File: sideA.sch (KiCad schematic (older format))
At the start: 16 parts

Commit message: Annotations and ERC error pending
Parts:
- gave numbers to parts that had none: 16
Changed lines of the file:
@@
-EESchema Schematic File Version 2  date Sun 16 Sep 2012 06:59:06 AM PDT
+EESchema Schematic File Version 2  date Tue 18 Sep 2012 12:09:37 PM PDT
 LIBS:power
 LIBS:device
@@
 Sheet 1 1
 Title "SMT4dummies - sideA"
-Date "16 sep 2012"
+Date "18 sep 2012"
 Rev ""
 Comp "d-Squared Robotics"
@@
 Comment4 ""
 $EndDescr
+Wire Wire Line
+	3550 2100 3650 2100
+Wire Bus Line
+	800  3300 800  800
+Wire Bus Line
+	800  3300 3000 3300
+Wire Bus Line
+	800  800  3000 800
+Wire Wire Line
+	1150 1050 2650 1050
+Wire Wire Line
+	5650 1150 5650 1050
+Connection ~ 4150 3650
+Wire Wire Line
+	4150 3650 4150 3000
+Connection ~ 5250 3650
+Wire Wire Line
+	5250 3550 5250 3650
+Wire Wire Line
+	3650 3650 5650 3650
+Connection ~ 4500 2300
+Wire Wire Line
+	4500 2950 4500 2300
+Wire Wire Line
+	3850 2800 3750 2800
+Wire Wire Line
+	3750 2800 3750 2300
+Wire Wire Line
+	3750 2300 4600 2300
+Wire Wire Line
+	5650 1550 5650 1650
+Wire Wire Line
+	5100 2500 5250 2500
+Wire Wire Line
+	5350 2800 5250 2800
+Connection ~ 4150 2500
+Connection ~ 1650 3050
+Wire Wire Line
+	1650 2950 1650 3050
+Wire Wire Line
+	2650 1650 2650 1550
+Wire Wire Line
+	2250 2450 2350 2450
+Wire Wire Line
+	1650 2150 1650 2550
+Wire Wire Line
+	1050 1850 1150 1850
+Wire Wire Line
+	1150 1850 1150 1050
+Wire Wire Line
+	2650 1050 2650 1150
+Wire Wire Line
+	1650 1550 1650 1050
+Connection ~ 1650 1050
+Wire Wire Line
+	1750 2450 1650 2450
+Connection ~ 1650 2450
+Wire Wire Line
+	2650 2250 2650 2150
+Wire Wire Line
+	2650 2650 2650 3050
+Wire Wire Line
+	1150 2050 1150 3050
+Wire Wire Line
+	1150 2050 1000 2050
+Wire Wire Line
+	4150 2150 4150 2600
+Wire Wire Line
+	4150 1550 4150 1650
+Wire Wire Line
+	5100 2300 5650 2300
+Wire Wire Line
+	5650 2150 5650 2600
+Connection ~ 5650 2300
+Wire Wire Line
+	5250 2500 5250 2950
+Connection ~ 5250 2800
+Wire Wire Line
+	3650 3650 3650 2300
+Wire Wire Line
+	5650 3650 5650 3000
+Wire Wire Line
+	4500 3550 4500 3650
+Connection ~ 4500 3650
+Wire Wire Line
+	4150 1050 4150 1150
+Wire Wire Line
+	1150 3050 2650 3050
+Wire Wire Line
+	4600 2500 4150 2500
+Wire Wire Line
+	3650 2100 3650 1050
+Wire Wire Line
+	3650 1050 5650 1050
+Connection ~ 4150 1050
+Wire Bus Line
+	3000 800  3000 3300
+Wire Bus Line
+	3300 3900 6050 3900
+Wire Bus Line
+	3300 3900 3300 800
+Wire Bus Line
+	6050 3900 6050 800
 Wire Bus Line
 	6050 800  3300 800
-Wire Bus Line
-	6050 800  6050 3900
-Wire Bus Line
-	3300 800  3300 3900
-Wire Bus Line
-	3300 3900 6050 3900
-Wire Bus Line
-	3000 800  3000 3300
-Connection ~ 4150 1050
-Wire Wire Line
-	3650 1050 5650 1050
-Wire Wire Line
-	3500 2300 3650 2300
-Wire Wire Line
-	3650 1050 3650 2100
-Wire Wire Line
-	4600 2500 4150 2500
-Wire Wire Line
-	1150 3050 2650 3050
-Wire Wire Line
-	4150 1050 4150 1150
-Connection ~ 4500 3650
-Wire Wire Line
-	4500 3550 4500 3650
-Wire Wire Line
-	5650 3000 5650 3650
-Wire Wire Line
-	3650 2300 3650 3650
-Connection ~ 5250 2800
-Wire Wire Line
-	5250 2950 5250 2500
-Connection ~ 5650 2300
-Wire Wire Line
-	5650 2150 5650 2600
-Wire Wire Line
-	5100 2300 5650 2300
-Wire Wire Line
-	4150 1550 4150 1650
-Wire Wire Line
-	4150 2150 4150 2600
-Wire Wire Line
-	1000 2050 1150 2050
-Wire Wire Line
-	1150 2050 1150 3050
-Wire Wire Line
-	2650 3050 2650 2650
-Wire Wire Line
-	2650 2250 2650 2150
-Connection ~ 1650 2450
-Wire Wire Line
-	1750 2450 1650 2450
-Connection ~ 1650 1050
-Wire Wire Line
-	1650 1550 1650 1050
-Wire Wire Line
-	2650 1150 2650 1050
-Wire Wire Line
-	1150 1850 1150 1050
-Wire Wire Line
-	1150 1850 1050 1850
-Wire Wire Line
-	1650 2150 1650 2550
-Wire Wire Line
-	2250 2450 2350 2450
-Wire Wire Line
-	2650 1650 2650 1550
-Wire Wire Line
-	1650 2950 1650 3050
-Connection ~ 1650 3050
-Connection ~ 4150 2500
-Wire Wire Line
-	5350 2800 5250 2800
-Wire Wire Line
-	5250 2500 5100 2500
-Wire Wire Line
-	5650 1550 5650 1650
-Wire Wire Line
-	4600 2300 3750 2300
-Wire Wire Line
-	3750 2300 3750 2800
-Wire Wire Line
-	3750 2800 3850 2800
-Wire Wire Line
-	4500 2950 4500 2300
-Connection ~ 4500 2300
-Wire Wire Line
-	3650 3650 5650 3650
-Wire Wire Line
-	5250 3550 5250 3650
-Connection ~ 5250 3650
-Wire Wire Line
-	4150 3650 4150 3000
-Connection ~ 4150 3650
-Wire Wire Line
-	5650 1050 5650 1150
-Wire Wire Line
-	1150 1050 2650 1050
-Wire Wire Line
-	3650 2100 3550 2100
-Wire Bus Line
-	3000 800  800  800
-Wire Bus Line
-	3000 3300 800  3300
-Wire Bus Line
-	800  3300 800  800
+Wire Wire Line
+	3650 2300 3500 2300
 Text Notes 5600 3850 0    60   ~ 0
 Memory\n
 $Comp
-L SW_PUSH SW?
+L SW_PUSH SW2
 U 1 1 5055BB35
 P 4500 3250
-F 0 "SW?" H 4650 3360 50  0000 C CNN
+F 0 "SW2" H 4650 3360 50  0000 C CNN
 F 1 "SW_PUSH" H 4500 3170 50  0000 C CNN
 	1    4500 3250
@@
 $EndComp
 $Comp
-L SW_PUSH SW?
+L SW_PUSH SW3
 U 1 1 5055BB28
 P 5250 3250
-F 0 "SW?" H 5400 3360 50  0000 C CNN
+F 0 "SW3" H 5400 3360 50  0000 C CNN
 F 1 "SW_PUSH" H 5250 3170 50  0000 C CNN
 	1    5250 3250
@@
 $EndComp
 $Comp
-L R R?
+L R R4
 U 1 1 5055B3BC
 P 4850 2300
-F 0 "R?" V 4930 2300 50  0000 C CNN
+F 0 "R4" V 4930 2300 50  0000 C CNN
 F 1 "R" V 4850 2300 50  0000 C CNN
 	1    4850 2300
@@
 $EndComp
 $Comp
-L R R?
+L R R5
 U 1 1 5055B3AE
 P 4850 2500
-F 0 "R?" V 4930 2500 50  0000 C CNN
+F 0 "R5" V 4930 2500 50  0000 C CNN
 F 1 "R" V 4850 2500 50  0000 C CNN
 	1    4850 2500
@@
 $EndComp
 $Comp
-L BC237 Q?
+L BC237 Q3
 U 1 1 5055B0D0
 P 5550 2800
-F 0 "Q?" H 5750 2700 50  0000 C CNN
+F 0 "Q3" H 5750 2700 50  0000 C CNN
 F 1 "BC237" H 5800 2950 50  0000 C CNN
 F 2 "TO92-EBC" H 5740 2800 30  0001 C CNN
@@
 $EndComp
 $Comp
-L BC237 Q?
+L BC237 Q2
 U 1 1 5055B0B6
 P 4050 2800
-F 0 "Q?" H 4250 2700 50  0000 C CNN
+F 0 "Q2" H 4250 2700 50  0000 C CNN
 F 1 "BC237" H 4300 2950 50  0000 C CNN
 F 2 "TO92-EBC" H 4240 2800 30  0001 C CNN
@@
 $EndComp
 $Comp
-L R R?
+L R R6
 U 1 1 5055AFCE
 P 5650 1900
-F 0 "R?" V 5730 1900 50  0000 C CNN
+F 0 "R6" V 5730 1900 50  0000 C CNN
 F 1 "R" V 5650 1900 50  0000 C CNN
 	1    5650 1900
@@
 $EndComp
 $Comp
-L R R?
+L R R3
 U 1 1 5055AFCA
 P 4150 1900
-F 0 "R?" V 4230 1900 50  0000 C CNN
+F 0 "R3" V 4230 1900 50  0000 C CNN
 F 1 "R" V 4150 1900 50  0000 C CNN
 	1    4150 1900
@@
 $EndComp
 $Comp
-L LED D?
+L LED D3
 U 1 1 5055AFBC
 P 5650 1350
-F 0 "D?" H 5650 1450 50  0000 C CNN
+F 0 "D3" H 5650 1450 50  0000 C CNN
 F 1 "LED" H 5650 1250 50  0000 C CNN
 	1    5650 1350
@@
 $EndComp
 $Comp
-L LED D?
+L LED D2
 U 1 1 5051E656
 P 4150 1350
-F 0 "D?" H 4150 1450 50  0000 C CNN
+F 0 "D2" H 4150 1450 50  0000 C CNN
 F 1 "LED" H 4150 1250 50  0000 C CNN
 	1    4150 1350
@@
 $EndComp
 $Comp
-L R R?
+L R R1
 U 1 1 5051AD8C
 P 2000 2450
-F 0 "R?" V 2080 2450 50  0000 C CNN
+F 0 "R1" V 2080 2450 50  0000 C CNN
 F 1 "R" V 2000 2450 50  0000 C CNN
 	1    2000 2450
@@
 $EndComp
 $Comp
-L BC237 Q?
+L BC237 Q1
 U 1 1 5051AD26
 P 2550 2450
-F 0 "Q?" H 2750 2350 50  0000 C CNN
+F 0 "Q1" H 2750 2350 50  0000 C CNN
 F 1 "BC237" H 2800 2600 50  0000 C CNN
 F 2 "TO92-EBC" H 2740 2450 30  0001 C CNN
@@
 $EndComp
 $Comp
-L SW_PUSH SW?
+L SW_PUSH SW1
 U 1 1 5051AC01
 P 1650 1850
-F 0 "SW?" H 1800 1960 50  0000 C CNN
+F 0 "SW1" H 1800 1960 50  0000 C CNN
 F 1 "SW_PUSH" H 1650 1770 50  0000 C CNN
 	1    1650 1850
@@
 $EndComp
 $Comp
-L LED D?
+L LED D1
 U 1 1 5051A946
 P 2650 1350
-F 0 "D?" H 2650 1450 50  0000 C CNN
+F 0 "D1" H 2650 1450 50  0000 C CNN
 F 1 "LED" H 2650 1250 50  0000 C CNN
 	1    2650 1350
@@
 $EndComp
 $Comp
-L CP1 C?
+L CP1 C1
 U 1 1 5051A92A
 P 1650 2750
-F 0 "C?" H 1700 2850 50  0000 L CNN
+F 0 "C1" H 1700 2850 50  0000 L CNN
 F 1 "CP1" H 1700 2650 50  0000 L CNN
 	1    1650 2750
@@
 $EndComp
 $Comp
-L R R?
+L R R2
 U 1 1 5051A90B
 P 2650 1900
-F 0 "R?" V 2730 1900 50  0000 C CNN
+F 0 "R2" V 2730 1900 50  0000 C CNN
 F 1 "R" V 2650 1900 50  0000 C CNN
 	1    2650 1900

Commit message: Annotated and ERC checked
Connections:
- wire segments 40 -> 42
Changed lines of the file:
@@
-EESchema Schematic File Version 2  date Tue 18 Sep 2012 12:09:37 PM PDT
+EESchema Schematic File Version 2  date Tue 18 Sep 2012 12:41:14 PM PDT
 LIBS:power
 LIBS:device
@@
 Comment4 ""
 $EndDescr
-Wire Wire Line
-	3550 2100 3650 2100
+Wire Bus Line
+	6300 1450 6300 800
+Wire Bus Line
+	6300 1450 6850 1450
+Wire Bus Line
+	6850 1450 6850 800
+Wire Bus Line
+	6850 800  6300 800
+Wire Wire Line
+	6450 1100 6450 1200
+Wire Wire Line
+	3500 2300 3650 2300
+Wire Bus Line
+	6050 800  3300 800
+Wire Bus Line
+	6050 800  6050 3900
+Wire Bus Line
+	3300 800  3300 3900
+Wire Bus Line
+	3300 3900 6050 3900
+Wire Bus Line
+	3000 800  3000 3300
+Connection ~ 4150 1050
+Wire Wire Line
+	3650 1050 5650 1050
+Wire Wire Line
+	3650 1050 3650 2100
+Wire Wire Line
+	4600 2500 4150 2500
+Wire Wire Line
+	1150 3050 2650 3050
+Wire Wire Line
+	4150 1050 4150 1150
+Connection ~ 4500 3650
+Wire Wire Line
+	4500 3550 4500 3650
+Wire Wire Line
+	5650 3000 5650 3650
+Wire Wire Line
+	3650 2300 3650 3650
+Connection ~ 5250 2800
+Wire Wire Line
+	5250 2950 5250 2500
+Connection ~ 5650 2300
+Wire Wire Line
+	5650 2150 5650 2600
+Wire Wire Line
+	5100 2300 5650 2300
+Wire Wire Line
+	4150 1550 4150 1650
+Wire Wire Line
+	4150 2150 4150 2600
+Wire Wire Line
+	1000 2050 1150 2050
+Wire Wire Line
+	1150 2050 1150 3050
+Wire Wire Line
+	2650 3050 2650 2650
+Wire Wire Line
+	2650 2250 2650 2150
+Connection ~ 1650 2450
+Wire Wire Line
+	1750 2450 1650 2450
+Connection ~ 1650 1050
+Wire Wire Line
+	1650 1550 1650 1050
+Wire Wire Line
+	2650 1150 2650 1050
+Wire Wire Line
+	1150 1850 1150 1050
+Wire Wire Line
+	1150 1850 1050 1850
+Wire Wire Line
+	1650 2150 1650 2550
+Wire Wire Line
+	2250 2450 2350 2450
+Wire Wire Line
+	2650 1650 2650 1550
+Wire Wire Line
+	1650 2950 1650 3050
+Connection ~ 1650 3050
+Connection ~ 4150 2500
+Wire Wire Line
+	5350 2800 5250 2800
+Wire Wire Line
+	5250 2500 5100 2500
+Wire Wire Line
+	5650 1550 5650 1650
+Wire Wire Line
+	4600 2300 3750 2300
+Wire Wire Line
+	3750 2300 3750 2800
+Wire Wire Line
+	3750 2800 3850 2800
+Wire Wire Line
+	4500 2950 4500 2300
+Connection ~ 4500 2300
+Wire Wire Line
+	3650 3650 5650 3650
+Wire Wire Line
+	5250 3550 5250 3650
+Connection ~ 5250 3650
+Wire Wire Line
+	4150 3650 4150 3000
+Connection ~ 4150 3650
+Wire Wire Line
+	5650 1050 5650 1150
+Wire Wire Line
+	1150 1050 2650 1050
+Wire Bus Line
+	3000 800  800  800
+Wire Bus Line
+	3000 3300 800  3300
 Wire Bus Line
 	800  3300 800  800
-Wire Bus Line
-	800  3300 3000 3300
-Wire Bus Line
-	800  800  3000 800
-Wire Wire Line
-	1150 1050 2650 1050
-Wire Wire Line
-	5650 1150 5650 1050
-Connection ~ 4150 3650
-Wire Wire Line
-	4150 3650 4150 3000
-Connection ~ 5250 3650
-Wire Wire Line
-	5250 3550 5250 3650
-Wire Wire Line
-	3650 3650 5650 3650
-Connection ~ 4500 2300
-Wire Wire Line
-	4500 2950 4500 2300
-Wire Wire Line
-	3850 2800 3750 2800
-Wire Wire Line
-	3750 2800 3750 2300
-Wire Wire Line
-	3750 2300 4600 2300
-Wire Wire Line
-	5650 1550 5650 1650
-Wire Wire Line
-	5100 2500 5250 2500
-Wire Wire Line
-	5350 2800 5250 2800
-Connection ~ 4150 2500
-Connection ~ 1650 3050
-Wire Wire Line
-	1650 2950 1650 3050
-Wire Wire Line
-	2650 1650 2650 1550
-Wire Wire Line
-	2250 2450 2350 2450
-Wire Wire Line
-	1650 2150 1650 2550
-Wire Wire Line
-	1050 1850 1150 1850
-Wire Wire Line
-	1150 1850 1150 1050
-Wire Wire Line
-	2650 1050 2650 1150
-Wire Wire Line
-	1650 1550 1650 1050
-Connection ~ 1650 1050
-Wire Wire Line
-	1750 2450 1650 2450
-Connection ~ 1650 2450
-Wire Wire Line
-	2650 2250 2650 2150
-Wire Wire Line
-	2650 2650 2650 3050
-Wire Wire Line
-	1150 2050 1150 3050
-Wire Wire Line
-	1150 2050 1000 2050
-Wire Wire Line
-	4150 2150 4150 2600
-Wire Wire Line
-	4150 1550 4150 1650
-Wire Wire Line
-	5100 2300 5650 2300
-Wire Wire Line
-	5650 2150 5650 2600
-Connection ~ 5650 2300
-Wire Wire Line
-	5250 2500 5250 2950
-Connection ~ 5250 2800
-Wire Wire Line
-	3650 3650 3650 2300
-Wire Wire Line
-	5650 3650 5650 3000
-Wire Wire Line
-	4500 3550 4500 3650
-Connection ~ 4500 3650
-Wire Wire Line
-	4150 1050 4150 1150
-Wire Wire Line
-	1150 3050 2650 3050
-Wire Wire Line
-	4600 2500 4150 2500
-Wire Wire Line
-	3650 2100 3650 1050
-Wire Wire Line
-	3650 1050 5650 1050
-Connection ~ 4150 1050
-Wire Bus Line
-	3000 800  3000 3300
-Wire Bus Line
-	3300 3900 6050 3900
-Wire Bus Line
-	3300 3900 3300 800
-Wire Bus Line
-	6050 3900 6050 800
-Wire Bus Line
-	6050 800  3300 800
-Wire Wire Line
-	3650 2300 3500 2300
+Wire Wire Line
+	3650 2100 3550 2100
+Wire Wire Line
+	6700 950  6700 1100
+$Comp
+L PWR_FLAG #FLG01
+U 1 1 5058CE03
+P 6450 1100
+F 0 "#FLG01" H 6450 1370 30  0001 C CNN
+F 1 "PWR_FLAG" H 6450 1330 30  0000 C CNN
+	1    6450 1100
+	1    0    0    -1
+$EndComp
+$Comp
+L PWR_FLAG #FLG02
+U 1 1 5058CDFB
+P 6700 1100
+F 0 "#FLG02" H 6700 1370 30  0001 C CNN
+F 1 "PWR_FLAG" H 6700 1330 30  0000 C CNN
+	1    6700 1100
+	-1   0    0    1
+$EndComp
+$Comp
+L GND #PWR03
+U 1 1 5058CDC6
+P 6700 950
+F 0 "#PWR03" H 6700 950 30  0001 C CNN
+F 1 "GND" H 6700 880 30  0001 C CNN
+	1    6700 950
+	-1   0    0    1
+$EndComp
+$Comp
+L +5V #PWR04
+U 1 1 5058CDA4
+P 6450 1200
+F 0 "#PWR04" H 6450 1290 20  0001 C CNN
+F 1 "+5V" H 6450 1290 30  0000 C CNN
+	1    6450 1200
+	-1   0    0    1
+$EndComp
 Text Notes 5600 3850 0    60   ~ 0
 Memory\n
@@
 $EndComp
 $Comp
-L GND #PWR01
+L GND #PWR05
 U 1 1 5055B357
 P 3500 2300
-F 0 "#PWR01" H 3500 2300 30  0001 C CNN
+F 0 "#PWR05" H 3500 2300 30  0001 C CNN
 F 1 "GND" H 3500 2230 30  0001 C CNN
 	1    3500 2300
@@
 $EndComp
 $Comp
-L +5V #PWR02
+L +5V #PWR06
 U 1 1 5055B33A
 P 3550 2100
-F 0 "#PWR02" H 3550 2190 20  0001 C CNN
+F 0 "#PWR06" H 3550 2190 20  0001 C CNN
 F 1 "+5V" H 3550 2190 30  0000 C CNN
 	1    3550 2100
@@
 Time delay switch
 $Comp
-L GND #PWR03
+L GND #PWR07
 U 1 1 5051ADDA
 P 1000 2050
-F 0 "#PWR03" H 1000 2050 30  0001 C CNN
+F 0 "#PWR07" H 1000 2050 30  0001 C CNN
 F 1 "GND" H 1000 1980 30  0001 C CNN
 	1    1000 2050
@@
 $EndComp
 $Comp
-L +5V #PWR04
+L +5V #PWR08
 U 1 1 5051ADB7
 P 1050 1850
-F 0 "#PWR04" H 1050 1940 20  0001 C CNN
+F 0 "#PWR08" H 1050 1940 20  0001 C CNN
 F 1 "+5V" H 1050 1940 30  0000 C CNN
 	1    1050 1850

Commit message: Added USB power supply, ERC performed
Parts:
- added J1: USB_2, symbol USB_2
- added P1: CONN_2, symbol CONN_2
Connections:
- wire segments 42 -> 47
- no-connect marks 0 -> 2
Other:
- note added: "Power supply\n"
- note added: "Pwr flags\n"
- moved on the sheet: C1, D1, D2, D3, R1, R2, R3, R4, R5, R6, SW1, SW2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

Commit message: NPN transistors changed
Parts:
- removed Q1, Q2, Q3: BC237, TO92-EBC, symbol BC237
- added Q? (x3): NPN, symbol NPN
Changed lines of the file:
@@
-EESchema Schematic File Version 2  date Tue 18 Sep 2012 03:02:05 PM PDT
+EESchema Schematic File Version 2  date Mon 25 Feb 2013 02:33:02 PM CET
 LIBS:power
 LIBS:device
@@
 LIBS:contrib
 LIBS:valves
-LIBS:sideA-cache
 EELAYER 25  0
 EELAYER END
-$Descr A4 11700 8267
+$Descr A3 16535 11700
 encoding utf-8
 Sheet 1 1
 Title "SMT4dummies - sideA"
-Date "18 sep 2012"
+Date "25 feb 2013"
 Rev ""
 Comp "d-Squared Robotics"
@@
 Comment4 ""
 $EndDescr
+$Comp
+L NPN Q?
+U 1 1 512B64B2
+P 7250 3100
+F 0 "Q?" H 7250 2950 50  0000 R CNN
+F 1 "NPN" H 7250 3250 50  0000 R CNN
+	1    7250 3100
+	1    0    0    -1
+$EndComp
+$Comp
+L NPN Q?
+U 1 1 512B64AD
+P 5750 3100
+F 0 "Q?" H 5750 2950 50  0000 R CNN
+F 1 "NPN" H 5750 3250 50  0000 R CNN
+	1    5750 3100
+	1    0    0    -1
+$EndComp
+$Comp
+L NPN Q?
+U 1 1 512B64A4
+P 4250 2750
+F 0 "Q?" H 4250 2600 50  0000 R CNN
+F 1 "NPN" H 4250 2900 50  0000 R CNN
+	1    4250 2750
+	1    0    0    -1
+$EndComp
 Wire Bus Line
 	1100 2000 1100 1100
@@
 $EndComp
 $Comp
-L BC237 Q3
-U 1 1 5055B0D0
-P 7250 3100
-F 0 "Q3" H 7450 3000 50  0000 C CNN
-F 1 "BC237" H 7500 3250 50  0000 C CNN
-F 2 "TO92-EBC" H 7440 3100 30  0001 C CNN
-	1    7250 3100
-	1    0    0    -1
-$EndComp
-$Comp
-L BC237 Q2
-U 1 1 5055B0B6
-P 5750 3100
-F 0 "Q2" H 5950 3000 50  0000 C CNN
-F 1 "BC237" H 6000 3250 50  0000 C CNN
-F 2 "TO92-EBC" H 5940 3100 30  0001 C CNN
-	1    5750 3100
-	1    0    0    -1
-$EndComp
-$Comp
 L R R6
 U 1 1 5055AFCE
@@
 $EndComp
 $Comp
-L BC237 Q1
-U 1 1 5051AD26
-P 4250 2750
-F 0 "Q1" H 4450 2650 50  0000 C CNN
-F 1 "BC237" H 4500 2900 50  0000 C CNN
-F 2 "TO92-EBC" H 4440 2750 30  0001 C CNN
-	1    4250 2750
-	1    0    0    -1
-$EndComp
-$Comp

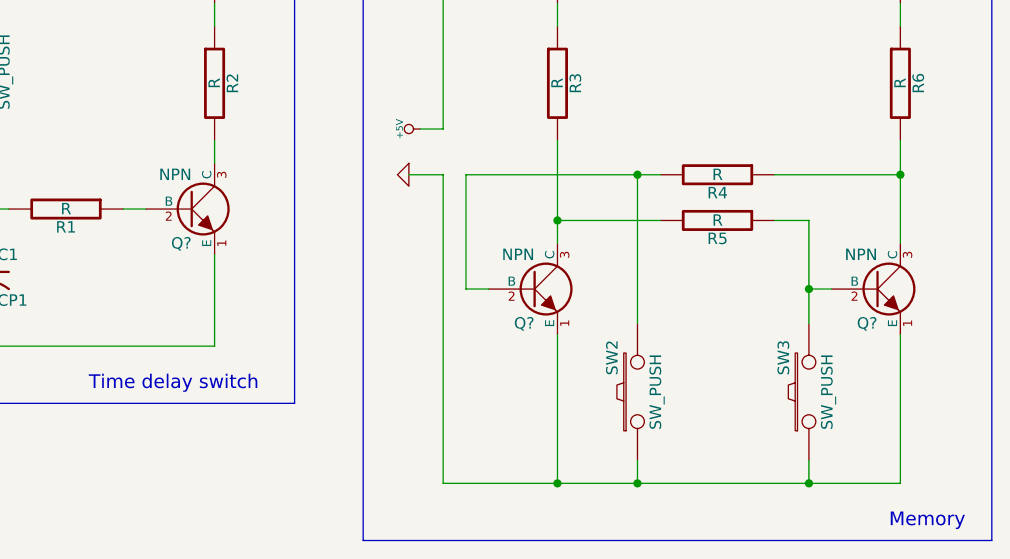
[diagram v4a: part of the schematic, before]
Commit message: Edited transistor pinout. Created new compoment NPN.
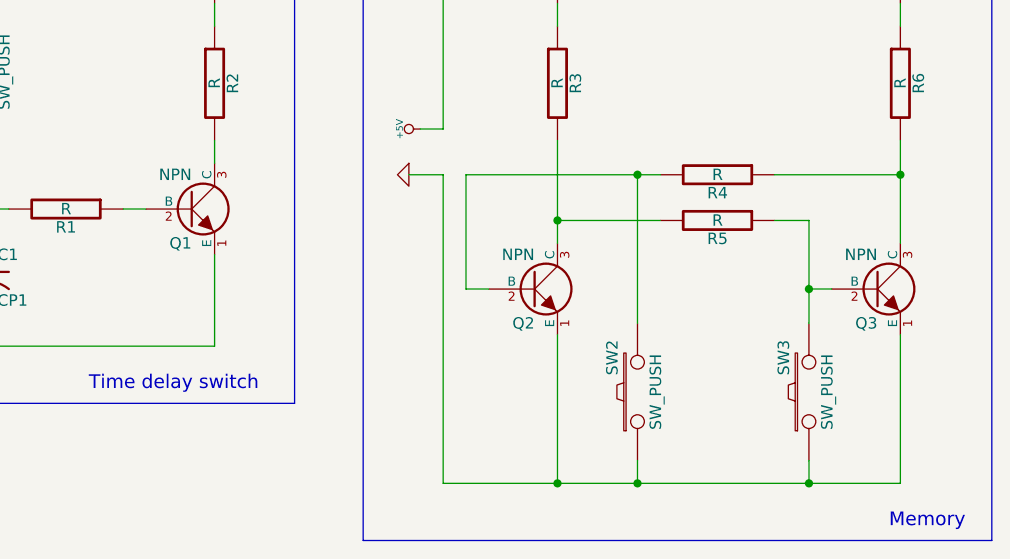
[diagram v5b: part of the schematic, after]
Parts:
- removed Q? (x3): NPN, symbol NPN
- added Q1, Q2, Q3: NPN, symbol NPN
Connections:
- net GND: now also Q1.1 (E), Q2.1 (E), Q3.1 (E)
- net at R2.2: now also Q1.3 (C)
- net at R1.1: now also Q1.2 (B)
- net at R3.2, R5.2: now also Q2.3 (C)
- net at R4.1, R6.2: now also Q3.3 (C)
- net at R5.1, SW3.2: now also Q3.2 (B)
- net at R4.2, SW2.2: now also Q2.2 (B)
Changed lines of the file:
@@
-EESchema Schematic File Version 2  date Mon 25 Feb 2013 02:33:02 PM CET
+EESchema Schematic File Version 2  date Tue 26 Feb 2013 22:33:32 CET
 LIBS:power
 LIBS:device
@@
 LIBS:contrib
 LIBS:valves
+LIBS:npn
+LIBS:sideA-cache
 EELAYER 25  0
 EELAYER END
@@
 Sheet 1 1
 Title "SMT4dummies - sideA"
-Date "25 feb 2013"
+Date "26 feb 2013"
 Rev ""
 Comp "d-Squared Robotics"
@@
 $EndDescr
 $Comp
-L NPN Q?
-U 1 1 512B64B2
+L NPN Q3
+U 1 1 512D29D8
 P 7250 3100
-F 0 "Q?" H 7250 2950 50  0000 R CNN
+F 0 "Q3" H 7250 2950 50  0000 R CNN
 F 1 "NPN" H 7250 3250 50  0000 R CNN
 	1    7250 3100
@@
 $EndComp
 $Comp
-L NPN Q?
-U 1 1 512B64AD
+L NPN Q2
+U 1 1 512D29D5
 P 5750 3100
-F 0 "Q?" H 5750 2950 50  0000 R CNN
+F 0 "Q2" H 5750 2950 50  0000 R CNN
 F 1 "NPN" H 5750 3250 50  0000 R CNN
 	1    5750 3100
@@
 $EndComp
 $Comp
-L NPN Q?
-U 1 1 512B64A4
+L NPN Q1
+U 1 1 512D29D2
 P 4250 2750
-F 0 "Q?" H 4250 2600 50  0000 R CNN
+F 0 "Q1" H 4250 2600 50  0000 R CNN
 F 1 "NPN" H 4250 2900 50  0000 R CNN
 	1    4250 2750
@@
 NoConn ~ 1500 1450
 $Comp
-L GND #PWR4
+L GND #PWR01
 U 1 1 5058EE8B
 P 1600 1750
-F 0 "#PWR4" H 1600 1750 30  0001 C CNN
+F 0 "#PWR01" H 1600 1750 30  0001 C CNN
 F 1 "GND" H 1600 1680 30  0001 C CNN
 	1    1600 1750
@@
 $EndComp
 $Comp
-L +5V #PWR3
+L +5V #PWR02
 U 1 1 5058EE6E
 P 1600 1250
-F 0 "#PWR3" H 1600 1340 20  0001 C CNN
+F 0 "#PWR02" H 1600 1340 20  0001 C CNN
 F 1 "+5V" H 1600 1340 30  0000 C CNN
 	1    1600 1250
@@
 Pwr flags\n
 $Comp
-L PWR_FLAG #FLG1
+L PWR_FLAG #FLG03
 U 1 1 5058CE03
 P 1250 2550
-F 0 "#FLG1" H 1250 2820 30  0001 C CNN
+F 0 "#FLG03" H 1250 2820 30  0001 C CNN
 F 1 "PWR_FLAG" H 1250 2780 30  0000 C CNN
 	1    1250 2550
@@
 $EndComp
 $Comp
-L PWR_FLAG #FLG2
+L PWR_FLAG #FLG04
 U 1 1 5058CDFB
 P 1500 2550
-F 0 "#FLG2" H 1500 2820 30  0001 C CNN
+F 0 "#FLG04" H 1500 2820 30  0001 C CNN
 F 1 "PWR_FLAG" H 1500 2780 30  0000 C CNN
 	1    1500 2550
@@
 $EndComp
 $Comp
-L GND #PWR2
+L GND #PWR05
 U 1 1 5058CDC6
 P 1500 2400
-F 0 "#PWR2" H 1500 2400 30  0001 C CNN
+F 0 "#PWR05" H 1500 2400 30  0001 C CNN
 F 1 "GND" H 1500 2330 30  0001 C CNN
 	1    1500 2400
@@
 $EndComp
 $Comp
-L +5V #PWR1
+L +5V #PWR06
 U 1 1 5058CDA4
 P 1250 2650
-F 0 "#PWR1" H 1250 2740 20  0001 C CNN
+F 0 "#PWR06" H 1250 2740 20  0001 C CNN
 F 1 "+5V" H 1250 2740 30  0000 C CNN
 	1    1250 2650
@@
 $EndComp
 $Comp
-L GND #PWR7
+L GND #PWR07
 U 1 1 5055B357
 P 5200 2600
-F 0 "#PWR7" H 5200 2600 30  0001 C CNN
+F 0 "#PWR07" H 5200 2600 30  0001 C CNN
 F 1 "GND" H 5200 2530 30  0001 C CNN
 	1    5200 2600
@@
 $EndComp
 $Comp
-L +5V #PWR8
+L +5V #PWR08
 U 1 1 5055B33A
 P 5250 2400
-F 0 "#PWR8" H 5250 2490 20  0001 C CNN
+F 0 "#PWR08" H 5250 2490 20  0001 C CNN
 F 1 "+5V" H 5250 2490 30  0000 C CNN
 	1    5250 2400
@@
 Time delay switch
 $Comp
-L GND #PWR5
+L GND #PWR09
 U 1 1 5051ADDA
 P 2700 2350
-F 0 "#PWR5" H 2700 2350 30  0001 C CNN
+F 0 "#PWR09" H 2700 2350 30  0001 C CNN
 F 1 "GND" H 2700 2280 30  0001 C CNN
 	1    2700 2350
@@
 $EndComp
 $Comp
-L +5V #PWR6
+L +5V #PWR010
 U 1 1 5051ADB7
 P 2750 2150
-F 0 "#PWR6" H 2750 2240 20  0001 C CNN
+F 0 "#PWR010" H 2750 2240 20  0001 C CNN
 F 1 "+5V" H 2750 2240 30  0000 C CNN
 	1    2750 2150
